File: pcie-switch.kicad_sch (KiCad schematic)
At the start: 1 part, among them U1 PI7C9X3G606GPCFCAEX

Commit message: [#100765] Update subsheets
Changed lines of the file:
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@@
 	(generator_version "10.0")
 	(paper "A4")
+	(hierarchical_label "PCIe_{x2_0}{PCIe}"
+		(shape bidirectional)
+		(at 259.08 44.45 0)
+		(effects
+			(font
+				(size 1.27 1.27)
+			)
+			(justify left)
+		)
+	)
+	(hierarchical_label "PCIe_{x2_1}{PCIe}"
+		(shape bidirectional)
+		(at 259.08 49.53 0)
+		(effects
+			(font
+				(size 1.27 1.27)
+			)
+			(justify left)
+		)
+	)
+	(hierarchical_label "PCIe_{x2}{PCIe}"
+		(shape bidirectional)
+		(at 25.4 45.72 0)
+		(effects
+			(font
+				(size 1.27 1.27)
+			)
+			(justify left)
+		)
+	)
 	(symbol
 		(lib_id "antmicroInterfaceControllers:PI7C9X3G606GPCFCAEX")

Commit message: [#100765] Update symbol and tables
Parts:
- removed U1: PI7C9X3G606GPCFCAEX, antmicro-footprints:BGA-144_10x10mm_Layout12x12_P0.8mm, symbol antmicroInterfaceControllers:PI7C9X3G606GPCFCAEX
- added U1: PI7C9X3G606GP, antmicro-footprints:BGA-144_10x10mm_Layout12x12_P0.8mm, symbol antmicroInterfaceControllers:PI7C9X3G606GP
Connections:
- new net: U1.B1 (VSS), U1.B10 (VSS), U1.B4 (VSS), U1.B6 (VSS), U1.B7 (VSS), U1.B8 (VSS), U1.B9 (VSS), U1.D5 (VSS), U1.E6 (VSS), U1.E8 (VSS), U1.F11 (VSS), U1.F5 (VSS), U1.F7 (VSS), U1.G6 (VSS), U1.G8 (VSS), U1.H5 (VSS), U1.H7 (VSS), U1.J8 (VSS), U1.K11 (VSS), U1.K2 (VSS), U1.L10 (VSS), U1.L3 (VSS), U1.L4 (VSS), U1.L5 (VSS), U1.L8 (VSS), U1.L9 (VSS)

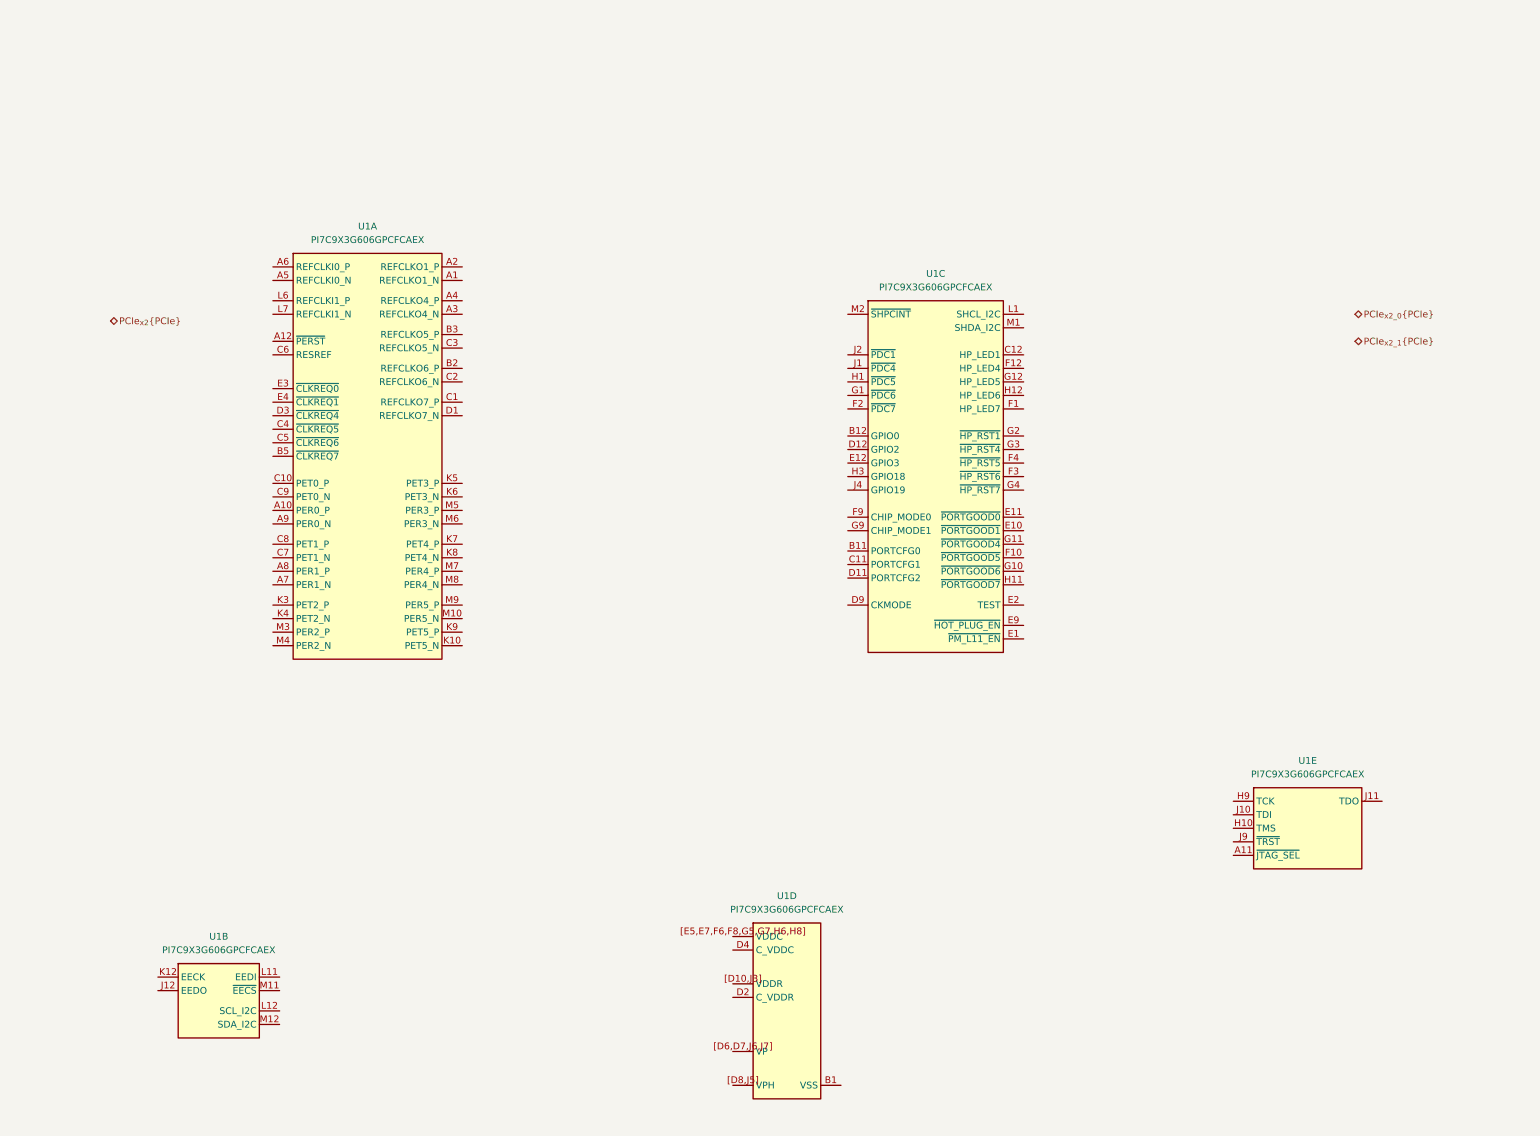
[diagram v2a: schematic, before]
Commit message: [#100765] Add PCIe connecions to M.2 slot A
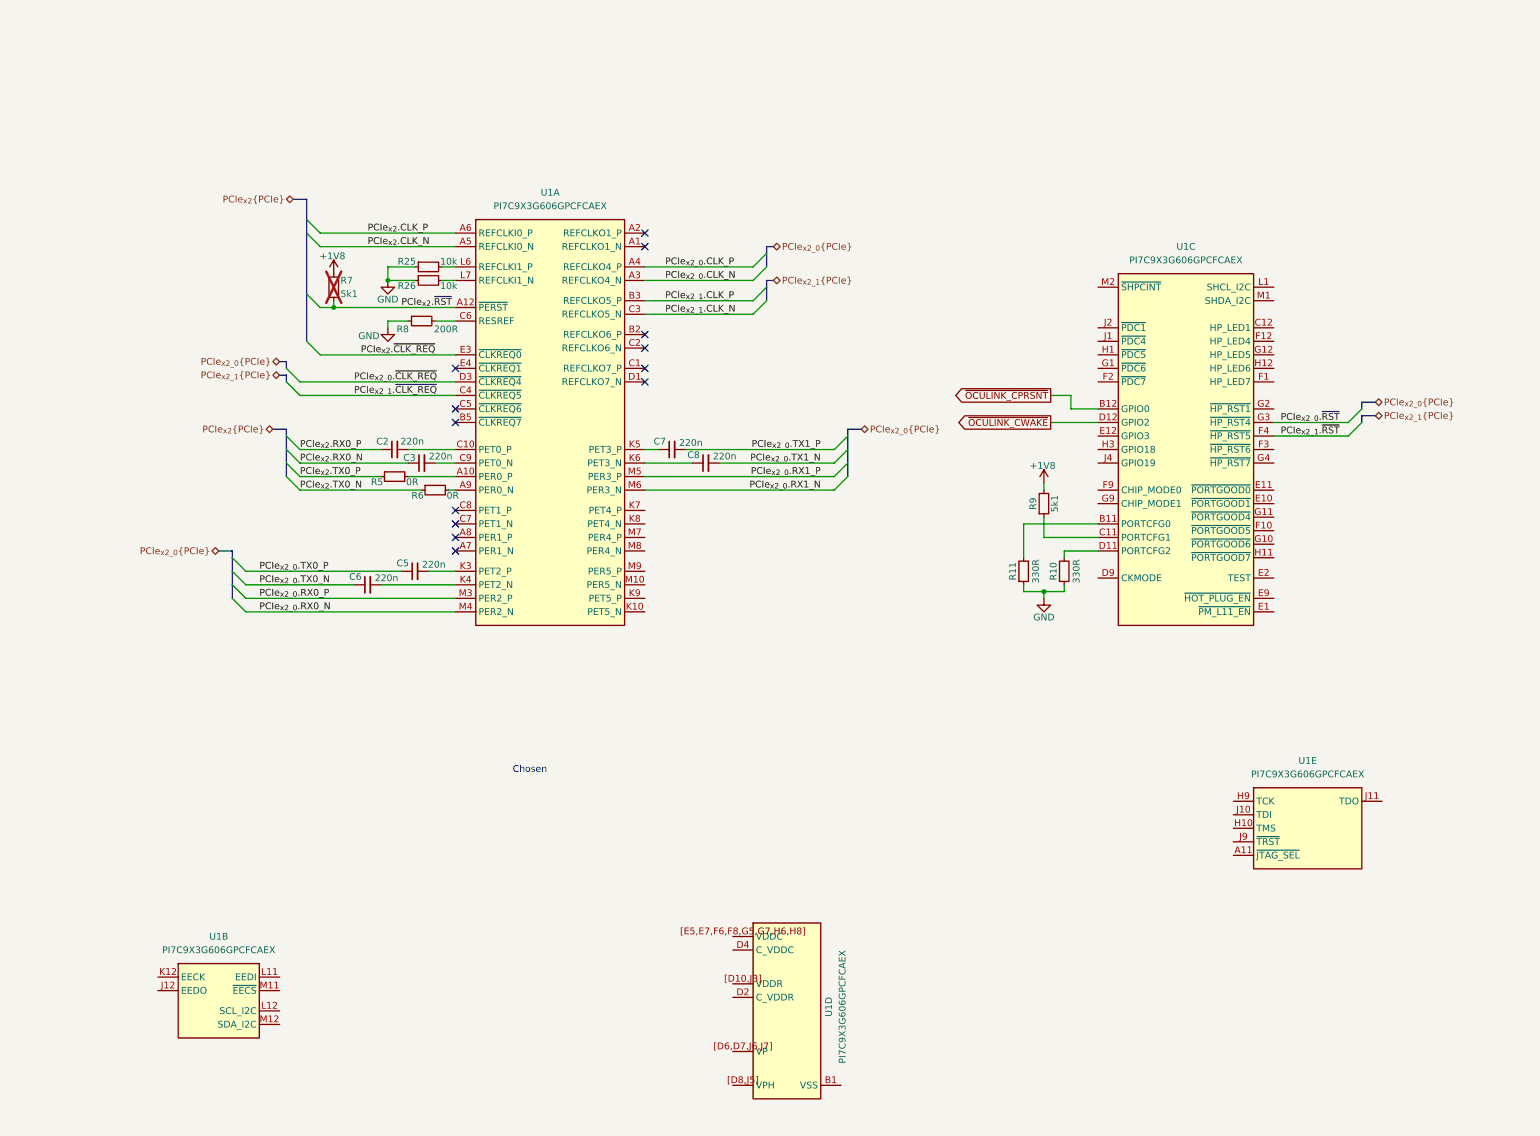
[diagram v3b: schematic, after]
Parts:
- added C2, C3, C5, C6, C7, C8: C_220n_0402, antmicro-footprints:C_0402_1005Metric, symbol antmicroCapacitors0402:C_220n_0402
- added R10, R11: R_330R_0402, antmicro-footprints:R_0402_1005Metric, symbol antmicroResistors0402:R_330R_0402
- added R25, R26: R_10k_0402, antmicro-footprints:R_0402_1005Metric, symbol antmicroResistors0402:R_10k_0402
- added R5, R6: R_0R_0402, antmicro-footprints:R_0402_1005Metric, symbol antmicroResistors0402:R_0R_0402
- added R7, R9: R_5k1_0402, antmicro-footprints:R_0402_1005Metric, symbol antmicroResistors0402:R_5k1_0402
- added R8: R_200R_0402, antmicro-footprints:R_0402_1005Metric, symbol antmicroResistors0402:R_200R_0402
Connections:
- net at U1.A10 (PER0_P): now also R5.2
- net PCIe_{x2}.~{RST}: now reaches U1.A12 (~{PERST})
- net PCIe_{x2}.~{RST}: now also R7.1
- net PCIe_{x2_0}.CLK_N: now reaches U1.A3 (REFCLKO4_N)
- net PCIe_{x2_0}.CLK_P: now reaches U1.A4 (REFCLKO4_P)
- net PCIe_{x2}.CLK_N: now reaches U1.A5 (REFCLKI0_N)
- net PCIe_{x2}.CLK_P: now reaches U1.A6 (REFCLKI0_P)
- net at U1.A9 (PER0_N): now also R6.2
- net PCIe_{x2_1}.CLK_P: now reaches U1.B3 (REFCLKO5_P)
- net at U1.C10 (PET0_P): now also C2.2
- net PCIe_{x2_1}.CLK_N: now reaches U1.C3 (REFCLKO5_N)
- net PCIe_{x2_1}.~{CLK_REQ}: now reaches U1.C4 (~{CLKREQ5})
- net at U1.C6 (RESREF): now also R8.2
- net at U1.C9 (PET0_N): now also C3.2
- net PCIe_{x2_0}.~{CLK_REQ}: now reaches U1.D3 (~{CLKREQ4})
- net PCIe_{x2}.~{CLK_REQ}: now reaches U1.E3 (~{CLKREQ0})
- net at U1.K3 (PET2_P): now also C5.2
- net at U1.K4 (PET2_N): now also C6.2
- net at U1.K5 (PET3_P): now also C7.1
- net at U1.K6 (PET3_N): now also C8.1
- net at U1.L6 (REFCLKI1_P): now also R25.2
- net at U1.L7 (REFCLKI1_N): now also R26.2
- net PCIe_{x2_0}.RX0_P: now reaches U1.M3 (PER2_P)
- net PCIe_{x2_0}.RX0_N: now reaches U1.M4 (PER2_N)
- net PCIe_{x2_0}.RX1_P: now reaches U1.M5 (PER3_P)
- net PCIe_{x2_0}.RX1_N: now reaches U1.M6 (PER3_N)
- net at U1.B11 (PORTCFG0): now also R11.2
- net ~{OCULINK_CPRSNT}: now reaches U1.B12 (GPIO0)
- net at U1.C11 (PORTCFG1): now also R9.1
- net at U1.D11 (PORTCFG2): now also R10.2
- net ~{OCULINK_CWAKE}: now reaches U1.D12 (GPIO2)
- net PCIe_{x2_1}.~{RST}: now reaches U1.F4 (~{HP_RST5})
- net PCIe_{x2_0}.~{RST}: now reaches U1.G3 (~{HP_RST4})
- new net +1V8: R7.2, R9.2
- new net GND: R10.1, R11.1, R25.1, R26.1, R8.1
- new net PCIe_{x2_0}.TX0_N: C6.1
- new net PCIe_{x2_0}.TX0_P: C5.1
- new net PCIe_{x2_0}.TX1_N: C8.2
- new net PCIe_{x2_0}.TX1_P: C7.2
- new net PCIe_{x2}.RX0_N: C3.1
- new net PCIe_{x2}.RX0_P: C2.1
- new net PCIe_{x2}.TX0_N: R6.1
- new net PCIe_{x2}.TX0_P: R5.1
- no-connect marks 0 -> 13
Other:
- note added: "Chosen"
- moved on the sheet: U1A, U1C

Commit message: [#100765] Update PCIe switch
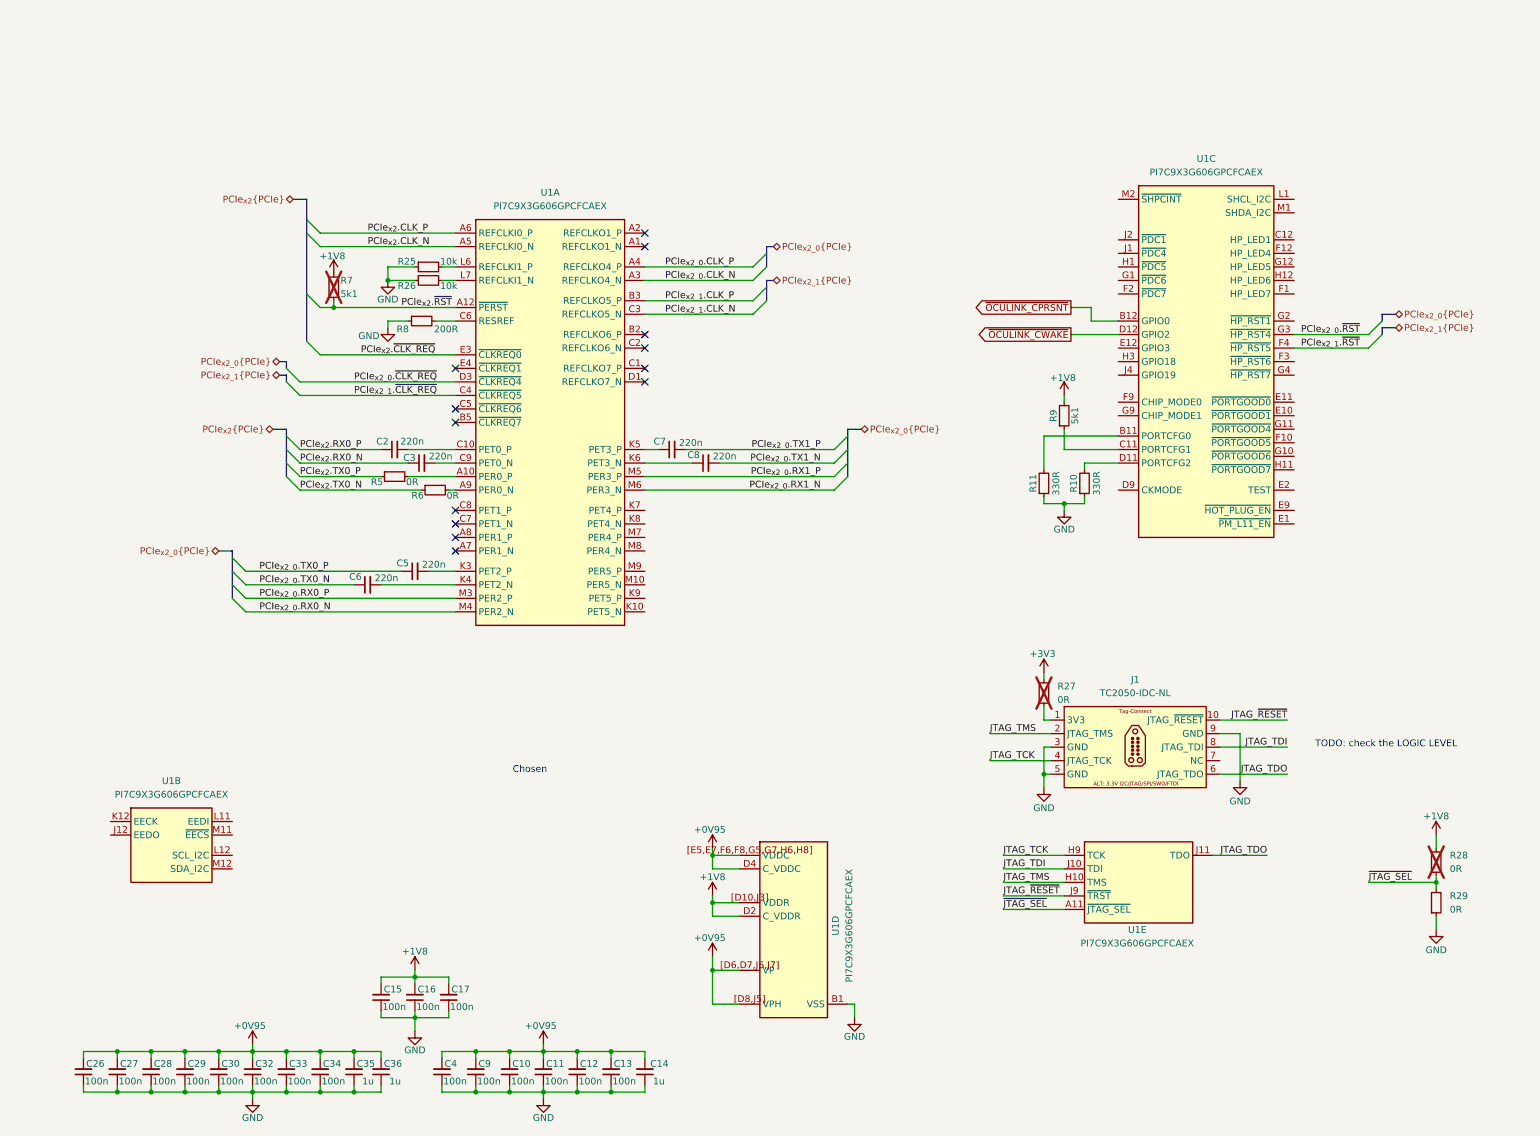
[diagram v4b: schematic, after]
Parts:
- added C10, C11, C12, C13, C15, C16, C17, C26, C27, C28, C29, C30, C32, C33, C34, C4, C9: C_100n_0402, antmicro-footprints:C_0402_1005Metric, symbol antmicroCapacitors0402:C_100n_0402
- added C14, C35, C36: C_1u_0402, antmicro-footprints:C_0402_1005Metric, symbol antmicroCapacitors0402:C_1u_0402
- added J1: Tag-Connect_TC2050-IDC-NL_2x5_P1.27mm, antmicro-footprints:Tag-Connect_TC2050-IDC-NL_2x5_P1.27mm, symbol antmicroTestPoints:Tag-Connect_TC2050-IDC-NL_2x5_P1.27mm
- added R27, R28, R29: R_0R_0402, antmicro-footprints:R_0402_1005Metric, symbol antmicroResistors0402:R_0R_0402
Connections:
- net +1V8: now also U1.D2 (C_VDDR), U1.[D10,J3] (VDDR), C15.2, C16.2, C17.2, R28.2
- net GND: now also U1.B1 (VSS), U1.B10 (VSS), U1.B4 (VSS), U1.B6 (VSS), U1.B7 (VSS), U1.B8 (VSS), U1.B9 (VSS), U1.D5 (VSS), U1.E6 (VSS), U1.E8 (VSS), U1.F11 (VSS), U1.F5 (VSS), U1.F7 (VSS), U1.G6 (VSS), U1.G8 (VSS), U1.H5 (VSS), U1.H7 (VSS), U1.J8 (VSS), U1.K11 (VSS), U1.K2 (VSS), U1.L10 (VSS), U1.L3 (VSS), U1.L4 (VSS), U1.L5 (VSS), U1.L8 (VSS), U1.L9 (VSS), C10.1, C11.1, C12.1, C13.1, C14.1, C15.1, C16.1, C17.1, C26.1, C27.1, C28.1, C29.1, C30.1, C32.1, C33.1, C34.1, C35.1, C36.1, C4.1, C9.1, J1.3, J1.5, J1.9, R29.1
- net +0V95: now reaches U1.D4 (C_VDDC)
- net +0V95: now also U1.[D6,D7,J6,J7] (VP), U1.[D8,J5] (VPH), U1.[E5,E7,F6,F8,G5,G7,H6,H8] (VDDC), C10.2, C11.2, C12.2, C13.2, C14.2, C26.2, C27.2, C28.2, C29.2, C30.2, C32.2, C33.2, C34.2, C35.2, C36.2, C4.2, C9.2
- net ~{JTAG_SEL}: now reaches U1.A11 (~{JTAG_SEL})
- net ~{JTAG_SEL}: now also R28.1, R29.2
- net JTAG_TMS: now reaches U1.H10 (TMS)
- net JTAG_TMS: now also J1.2
- net JTAG_TCK: now reaches U1.H9 (TCK)
- net JTAG_TCK: now also J1.4
- net JTAG_TDI: now reaches U1.J10 (TDI)
- net JTAG_TDI: now also J1.8
- net JTAG_TDO: now reaches U1.J11 (TDO)
- net JTAG_TDO: now also J1.6
- net JTAG_~{RESET}: now reaches U1.J9 (~{TRST})
- net JTAG_~{RESET}: now also J1.10
- new net: J1.1, R27.1
- new net +3V3: R27.2
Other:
- note added: "TODO: check the LOGIC LEVEL"
- moved on the sheet: R10, R11, R9, U1B, U1C, U1D, U1E

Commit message: [#100765] Update M.2 3V3 line
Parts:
- added C18, C20, C21, C22: C_220n_0402, antmicro-footprints:C_0402_1005Metric, symbol antmicroCapacitors0402:C_220n_0402
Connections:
- net at U1.K10 (PET5_N): now also C22.1
- net at U1.K7 (PET4_P): now also C18.1
- net at U1.K8 (PET4_N): now also C20.1
- net at U1.K9 (PET5_P): now also C21.1
- net PCIe_{x2_1}.RX0_N: now reaches U1.M10 (PER5_N)
- net PCIe_{x2_1}.RX0_N: now also U1.M8 (PER4_N)
- net PCIe_{x2_1}.RX0_P: now reaches U1.M7 (PER4_P)
- net PCIe_{x2_1}.RX0_P: now also U1.M9 (PER5_P)
- new net PCIe_{x2_1}.TX0_N: C20.2, C22.2
- new net PCIe_{x2_1}.TX0_P: C18.2, C21.2
